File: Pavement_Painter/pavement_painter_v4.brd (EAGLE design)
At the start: 62.6 x 110.3 mm, 76 parts, among them J3 POWER_JACK, Q1 TIP120, Q10 TIP120, Q11 TIP120, Q12 TIP120, Q13 TIP120, Q14 TIP120, Q15 TIP120, Q16 TIP120, Q2 TIP120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

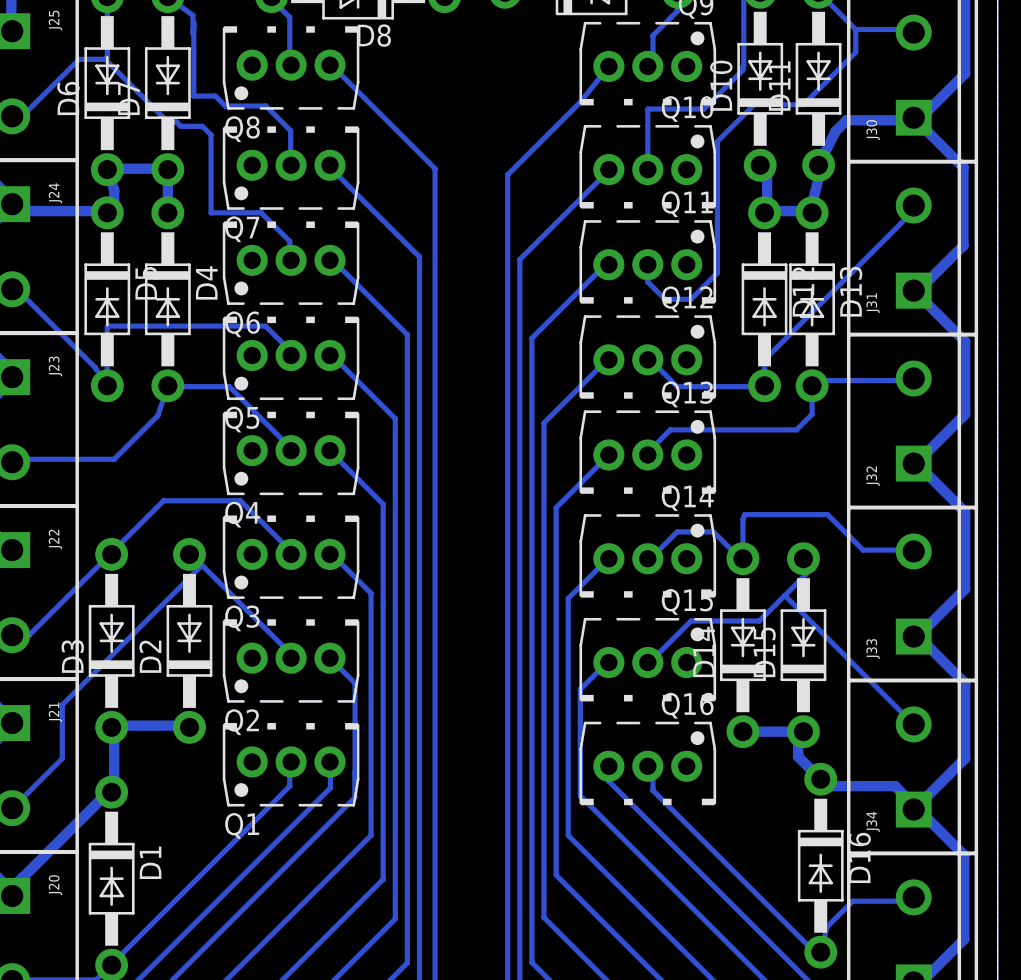
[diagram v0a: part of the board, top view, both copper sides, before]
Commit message: Minor layout updates
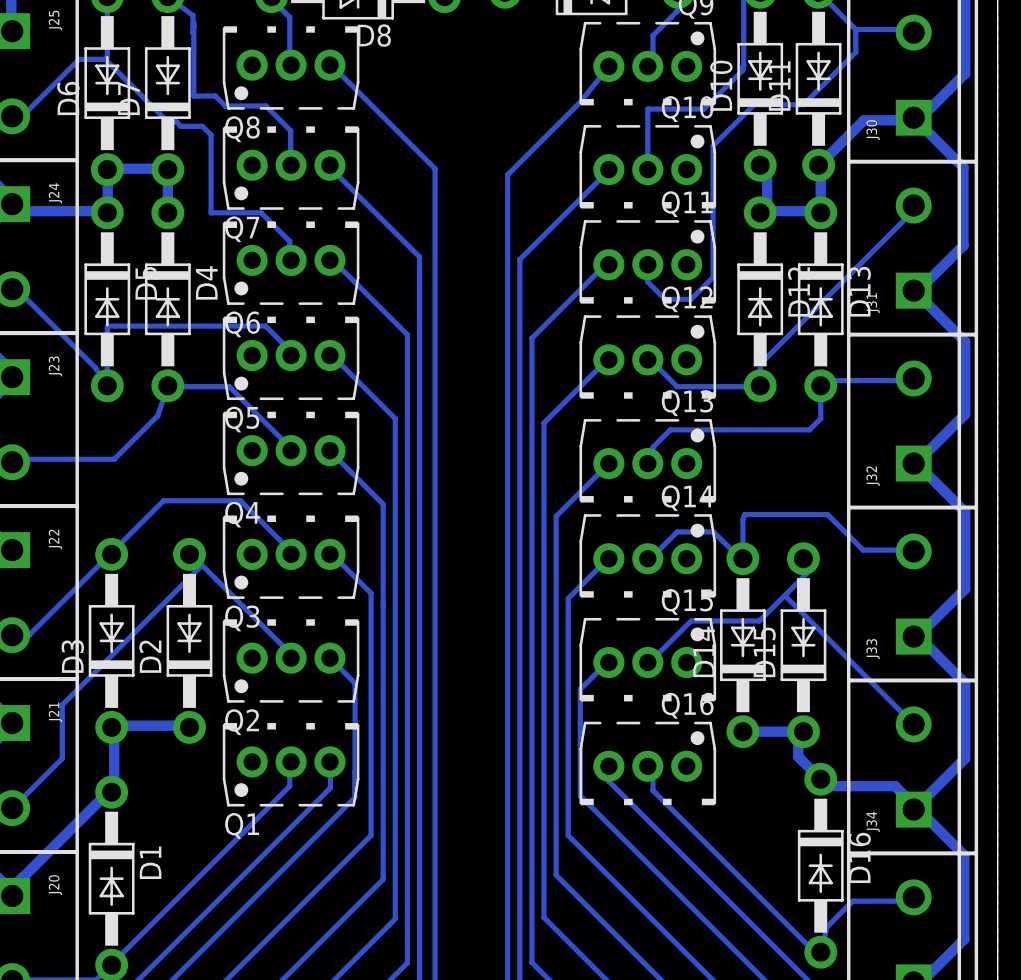
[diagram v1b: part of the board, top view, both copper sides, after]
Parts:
- moved D13 0.51 mm to (51.8, 64.5)
- moved Q13 0.51 mm to (41.7, 54.6)
- moved D12 0.25 mm to (48.3, 64.5)
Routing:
- net N$25: track 18.7 -> 19.4 mm
- net N$26: track 41.4 -> 40.9 mm
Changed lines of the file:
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@@
 </element>
 <element name="Q12" library="TIP120" package="BD679V" value="TIP120" x="41.656" y="60.706" rot="R180"/>
-<element name="D12" library="adafruit" library_urn="urn:adsk.eagle:library:420" package="DO41-10" package3d_urn="urn:adsk.eagle:package:6240344/1" value="1N4004" x="48.514" y="64.516" rot="R270"/>
+<element name="D12" library="adafruit" library_urn="urn:adsk.eagle:library:420" package="DO41-10" package3d_urn="urn:adsk.eagle:package:6240344/1" value="1N4004" x="48.26" y="64.516" rot="R270"/>
 <element name="R13" library="rcl" library_urn="urn:adsk.eagle:library:334" package="0207/10" package3d_urn="urn:adsk.eagle:package:23491/2" value="" x="47.117" y="14.732" rot="R90">
 <attribute name="SPICEPREFIX" value="R" x="56.007" y="-72.898" size="1.778" layer="27" rot="R90" display="off"/>
 </element>
-<element name="Q13" library="TIP120" package="BD679V" value="TIP120" x="41.656" y="55.118" rot="R180"/>
-<element name="D13" library="adafruit" library_urn="urn:adsk.eagle:library:420" package="DO41-10" package3d_urn="urn:adsk.eagle:package:6240344/1" value="1N4004" x="51.308" y="64.516" rot="R270"/>
+<element name="Q13" library="TIP120" package="BD679V" value="TIP120" x="41.656" y="54.61" rot="R180"/>
+<element name="D13" library="adafruit" library_urn="urn:adsk.eagle:library:420" package="DO41-10" package3d_urn="urn:adsk.eagle:package:6240344/1" value="1N4004" x="51.816" y="64.516" rot="R270"/>
 <element name="R14" library="rcl" library_urn="urn:adsk.eagle:library:334" package="0207/10" package3d_urn="urn:adsk.eagle:package:23491/2" value="" x="50.292" y="14.732" rot="R90">
 <attribute name="SPICEPREFIX" value="R" x="71.882" y="-98.298" size="1.778" layer="27" rot="R90" display="off"/>
@@
 <wire x1="4.2672" y1="39.4716" x2="1.016" y2="36.2204" width="0.6096" layer="16"/>
 <wire x1="4.2672" y1="39.4716" x2="4.318" y2="39.624" width="0.6096" layer="16"/>
-<wire x1="48.6664" y1="71.9836" x2="48.6664" y2="69.6976" width="0.6096" layer="16"/>
-<wire x1="48.6664" y1="69.6976" x2="48.514" y2="69.596" width="0.6096" layer="16"/>
-<wire x1="51.238275" y1="69.825096875" x2="51.689" y2="71.62801875" width="0.6096" layer="16"/>
-<wire x1="53.34" y1="75.0316" x2="57.2516" y2="75.0316" width="0.6096" layer="16"/>
-<wire x1="52.6796" y1="74.3712" x2="53.34" y2="75.0316" width="0.6096" layer="16"/>
+<wire x1="48.6664" y1="71.9836" x2="48.6664" y2="69.866934375" width="0.6096" layer="16"/>
+<wire x1="48.6664" y1="69.866934375" x2="48.26" y2="69.596" width="0.6096" layer="16"/>
+<wire x1="54.356" y1="75.0316" x2="57.2516" y2="75.0316" width="0.6096" layer="16"/>
+<wire x1="51.7144" y1="72.39" x2="54.356" y2="75.0316" width="0.6096" layer="16"/>
 <wire x1="57.2516" y1="75.0316" x2="57.277" y2="75.184" width="0.6096" layer="16"/>
-<wire x1="52.6796" y1="74.3712" x2="51.689" y2="72.39" width="0.6096" layer="16"/>
-<wire x1="51.1556" y1="69.6976" x2="48.6664" y2="69.6976" width="0.6096" layer="16"/>
-<wire x1="51.1556" y1="69.6976" x2="51.308" y2="69.596" width="0.6096" layer="16"/>
+<wire x1="51.6636" y1="69.6976" x2="48.6664" y2="69.6976" width="0.6096" layer="16"/>
+<wire x1="51.6636" y1="69.6976" x2="51.816" y2="69.596" width="0.6096" layer="16"/>
 <wire x1="60.2996" y1="57.7596" x2="57.404" y2="54.864" width="0.6096" layer="16"/>
 <wire x1="60.2996" y1="62.0268" x2="60.2996" y2="57.7596" width="0.6096" layer="16"/>
@@
 <wire x1="58.42" y1="89.027" x2="58.42" y2="89.2048" width="0.6096" layer="16"/>
 <wire x1="57.7088" y1="75.184" x2="57.277" y2="75.184" width="0.6096" layer="16"/>
-<wire x1="51.308" y1="69.596" x2="51.238275" y2="69.825096875" width="0.6096" layer="16"/>
-<wire x1="51.689" y1="71.62801875" x2="51.689" y2="72.39" width="0.6096" layer="16"/>
+<wire x1="51.816" y1="69.596" x2="51.816" y2="72.263" width="0.6096" layer="16"/>
 <wire x1="48.26" y1="72.39" x2="48.6664" y2="71.9836" width="0.6096" layer="16"/>
 <wire x1="10.3124" y1="39.116" x2="10.3124" y2="35.56" width="0.6096" layer="16"/>
@@
 <wire x1="14.5796" y1="39.4716" x2="14.732" y2="39.37" width="0.6096" layer="16"/>
 <wire x1="10.3124" y1="39.4716" x2="10.16" y2="39.37" width="0.6096" layer="16"/>
-<wire x1="10.3124" y1="70.9168" x2="10.3124" y2="69.866934375" width="0.6096" layer="16"/>
-<wire x1="10.3124" y1="69.866934375" x2="9.906" y2="69.596" width="0.6096" layer="16"/>
-<wire x1="10.3124" y1="70.9168" x2="9.906" y2="72.136" width="0.6096" layer="16"/>
+<wire x1="9.9314" y1="72.0598" x2="9.9314" y2="69.612934375" width="0.6096" layer="16"/>
+<wire x1="9.9314" y1="69.612934375" x2="9.906" y2="69.596" width="0.6096" layer="16"/>
+<wire x1="9.9314" y1="72.0598" x2="9.906" y2="72.136" width="0.6096" layer="16"/>
 <wire x1="10.16" y1="72.1868" x2="13.3096" y2="72.1868" width="0.6096" layer="16"/>
 <wire x1="13.3096" y1="72.1868" x2="13.462" y2="72.136" width="0.6096" layer="16"/>
@@
 <wire x1="22.7076" y1="84.582" x2="18.3896" y2="88.9" width="0.6096" layer="16"/>
 <wire x1="27.432" y1="84.582" x2="22.7076" y2="84.582" width="0.6096" layer="16"/>
+<wire x1="51.689" y1="72.39" x2="51.7144" y2="72.39" width="0.6096" layer="16"/>
+<wire x1="51.816" y1="72.263" x2="51.689" y2="72.39" width="0.6096" layer="16"/>
+<wire x1="48.6664" y1="69.866934375" x2="48.6664" y2="69.6976" width="0.6096" layer="16"/>
 </signal>
 <signal name="GND">
@@
 <contactref element="J30" pad="2"/>
 <wire x1="57.2516" y1="80.3656" x2="57.277" y2="80.184" width="0.3048" layer="16"/>
-<wire x1="45.7454" y1="66.0654" x2="44.196" y2="64.516" width="0.3048" layer="16"/>
+<wire x1="45.4914" y1="65.8114" x2="44.196" y2="64.516" width="0.3048" layer="16"/>
 <wire x1="44.196" y1="64.516" x2="42.672" y2="64.516" width="0.3048" layer="16"/>
 <wire x1="42.672" y1="64.516" x2="41.656" y2="65.532" width="0.3048" layer="16"/>
 <wire x1="41.656" y1="65.532" x2="41.656" y2="66.548" width="0.3048" layer="16"/>
-<wire x1="45.7454" y1="66.0654" x2="45.7454" y2="73.787" width="0.3048" layer="16"/>
+<wire x1="45.4914" y1="65.8114" x2="45.4914" y2="73.533" width="0.3048" layer="16"/>
 <wire x1="51.689" y1="82.55" x2="53.8734" y2="80.3656" width="0.3048" layer="16"/>
 <wire x1="53.8734" y1="80.3656" x2="57.2516" y2="80.3656" width="0.3048" layer="16"/>
-<wire x1="45.7454" y1="73.787" x2="47.9044" y2="75.946" width="0.3048" layer="16"/>
+<wire x1="45.4914" y1="73.533" x2="47.9044" y2="75.946" width="0.3048" layer="16"/>
 <wire x1="47.9044" y1="75.946" x2="50.8" y2="75.946" width="0.3048" layer="16"/>
 <wire x1="53.8734" y1="79.0194" x2="53.8734" y2="80.3656" width="0.3048" layer="16"/>
@@
 <contactref element="J31" pad="2"/>
 <wire x1="43.3832" y1="59.3852" x2="41.9608" y2="60.8076" width="0.3048" layer="16"/>
-<wire x1="48.3108" y1="59.3852" x2="43.3832" y2="59.3852" width="0.3048" layer="16"/>
+<wire x1="48.0568" y1="59.3852" x2="43.3832" y2="59.3852" width="0.3048" layer="16"/>
 <wire x1="41.9608" y1="60.8076" x2="41.656" y2="60.96" width="0.3048" layer="16"/>
-<wire x1="48.3108" y1="59.3852" x2="48.514" y2="59.436" width="0.3048" layer="16"/>
-<wire x1="48.514" y1="60.96" x2="57.2516" y2="69.6976" width="0.3048" layer="16"/>
+<wire x1="48.0568" y1="59.3852" x2="48.26" y2="59.436" width="0.3048" layer="16"/>
+<wire x1="48.26" y1="60.706" x2="57.2516" y2="69.6976" width="0.3048" layer="16"/>
 <wire x1="57.2516" y1="69.6976" x2="57.277" y2="70.024" width="0.3048" layer="16"/>
-<wire x1="48.514" y1="60.96" x2="48.514" y2="59.436" width="0.3048" layer="16"/>
+<wire x1="48.26" y1="60.706" x2="48.26" y2="59.436" width="0.3048" layer="16"/>
 </signal>
 <signal name="N$24">
@@
 <contactref element="Q13" pad="C"/>
 <contactref element="J32" pad="2"/>
-<wire x1="41.9608" y1="55.8292" x2="41.9608" y2="55.4736" width="0.3048" layer="16"/>
+<wire x1="41.9608" y1="55.8292" x2="41.9608" y2="54.9656" width="0.3048" layer="16"/>
 <wire x1="42.9768" y1="56.8452" x2="41.9608" y2="55.8292" width="0.3048" layer="16"/>
-<wire x1="50.3936" y1="56.8452" x2="42.9768" y2="56.8452" width="0.3048" layer="16"/>
-<wire x1="51.308" y1="57.7596" x2="50.3936" y2="56.8452" width="0.3048" layer="16"/>
-<wire x1="41.9608" y1="55.4736" x2="41.656" y2="55.372" width="0.3048" layer="16"/>
-<wire x1="51.5112" y1="59.7408" x2="57.2516" y2="59.7408" width="0.3048" layer="16"/>
+<wire x1="51.1556" y1="56.8452" x2="42.9768" y2="56.8452" width="0.3048" layer="16"/>
+<wire x1="51.816" y1="57.5056" x2="51.1556" y2="56.8452" width="0.3048" layer="16"/>
+<wire x1="41.9608" y1="54.9656" x2="41.656" y2="54.864" width="0.3048" layer="16"/>
+<wire x1="52.0192" y1="59.7408" x2="57.2516" y2="59.7408" width="0.3048" layer="16"/>
 <wire x1="57.2516" y1="59.7408" x2="57.277" y2="59.864" width="0.3048" layer="16"/>
-<wire x1="51.5112" y1="59.7408" x2="51.308" y2="59.436" width="0.3048" layer="16"/>
-<wire x1="51.308" y1="59.436" x2="51.308" y2="57.7596" width="0.3048" layer="16"/>
+<wire x1="52.0192" y1="59.7408" x2="51.816" y2="59.436" width="0.3048" layer="16"/>
+<wire x1="51.816" y1="59.436" x2="51.816" y2="57.5056" width="0.3048" layer="16"/>
 </signal>
 <signal name="N$26">
@@
 <contactref element="R13" pad="2"/>
 <wire x1="46.9392" y1="19.9136" x2="47.117" y2="19.812" width="0.3048" layer="16"/>
-<wire x1="39.37" y1="55.372" x2="36.2712" y2="52.2732" width="0.3048" layer="16"/>
-<wire x1="36.2712" y1="52.2732" x2="36.2712" y2="30.69215625" width="0.3048" layer="16"/>
+<wire x1="39.37" y1="54.864" x2="36.2712" y2="51.7652" width="0.3048" layer="16"/>
+<wire x1="36.2712" y1="51.7652" x2="36.2712" y2="30.69215625" width="0.3048" layer="16"/>
 <wire x1="36.2712" y1="30.69215625" x2="46.9392" y2="20.02415625" width="0.3048" layer="16"/>
 <wire x1="46.9392" y1="20.02415625" x2="46.9392" y2="19.9136" width="0.3048" layer="16"/>

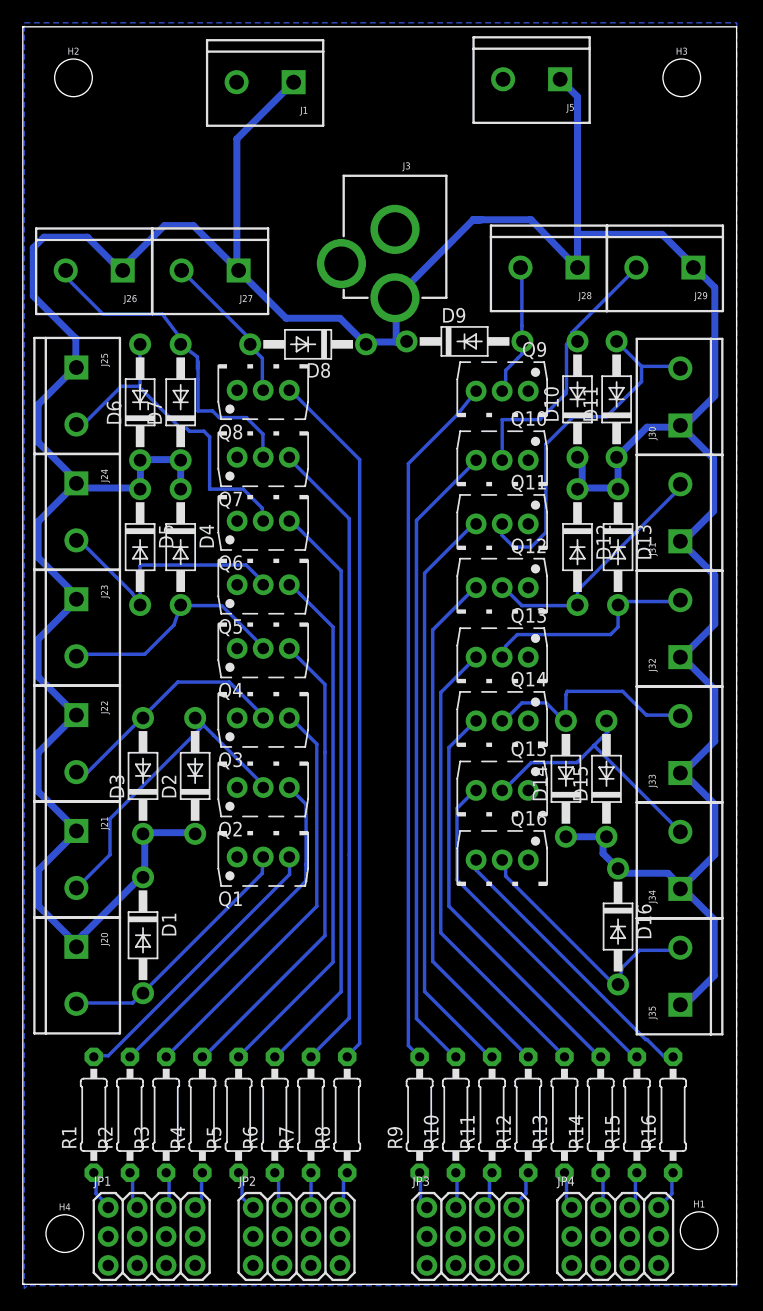
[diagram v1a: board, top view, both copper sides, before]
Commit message: Layout with tighter dimension
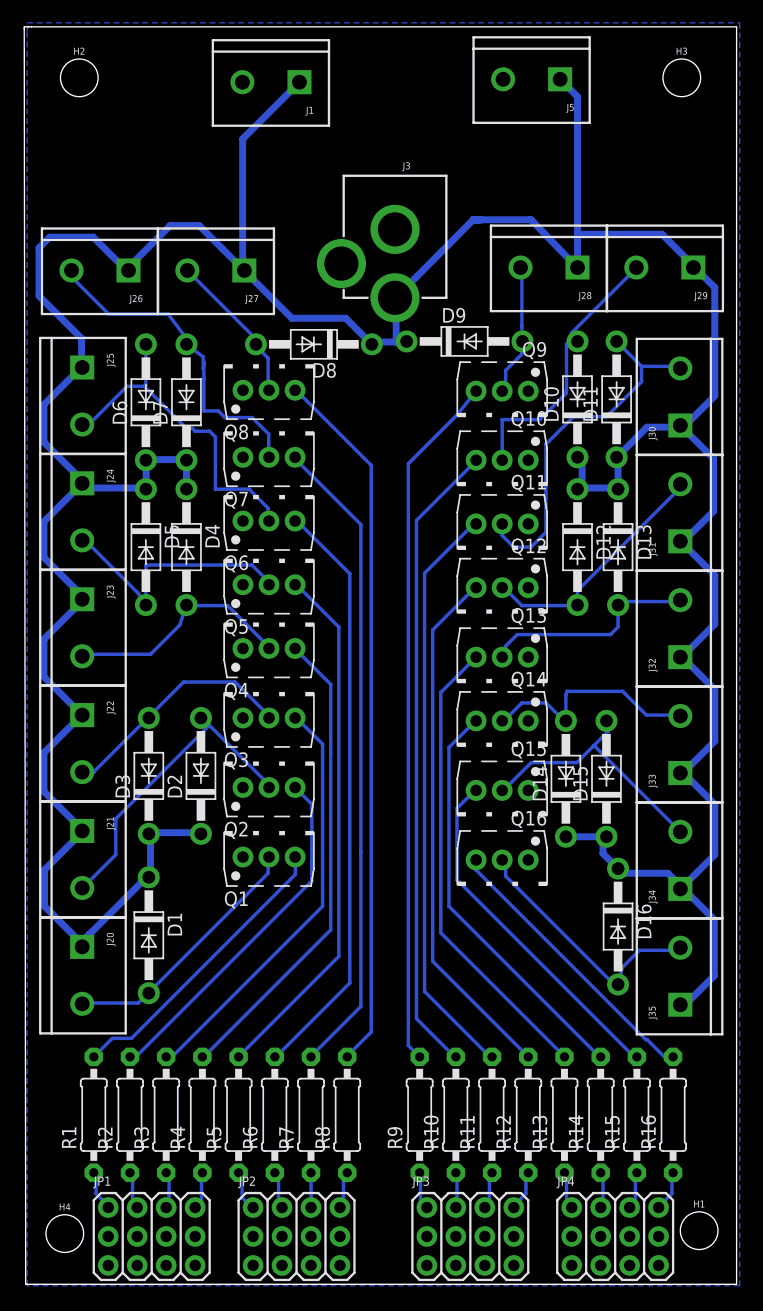
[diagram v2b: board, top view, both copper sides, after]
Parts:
- moved J1 0.51 mm to (23.9, 105.7)
- moved D2 0.51 mm to (15.2, 44.5)
- moved D4 0.51 mm to (14.0, 64.5)
- moved D7 0.51 mm to (14.0, 77.2)
- moved J26 0.51 mm to (8.89, 89.2)
- moved J20 0.51 mm to (4.45, 29.5)
- moved J21 0.51 mm to (4.45, 39.6)
- moved J22 0.51 mm to (4.45, 49.8)
- moved J23 0.51 mm to (4.45, 59.9)
- moved J24 0.51 mm to (4.45, 70.1)
- moved J25 0.51 mm to (4.45, 80.3)
- moved H2 0.51 mm to (4.57, 105.7)
- moved D1 0.51 mm to (10.7, 30.5)
- moved D3 0.51 mm to (10.7, 44.5)
- moved D5 0.51 mm to (10.4, 64.5)
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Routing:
- net N$5: track 22.1 -> 21.1 mm
- net N$16: track 61.5 -> 62.1 mm
- net N$14: track 56.2 -> 56.8 mm
- net +12V: track 334.8 -> 334.3 mm
- net N$4: track 25.3 -> 25.8 mm
- net N$2: track 30.6 -> 31.1 mm
- net N$6: track 36.3 -> 36.8 mm
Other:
- board size 62.6 x 110.3 mm -> 62.5 x 110.3 mm
